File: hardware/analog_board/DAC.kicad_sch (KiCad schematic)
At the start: 20 parts, among them U3 AD9747BCPZ

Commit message: feat: 滤波器&差分转单端电路原理图
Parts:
- added C100, C103, C104, C107, C108, C96: 10uF, Capacitor_SMD:C_0603_1608Metric, symbol Device:C
- added C101, C102, C105, C106, C91, C92, C93, C94, C98, C99: 100nF, Capacitor_SMD:C_0603_1608Metric, symbol Device:C
- added C61, C65, C75, C76: 56pF, Capacitor_SMD:C_0603_1608Metric, symbol Device:C
- added C62, C63, C66, C67, C79, C80, C83, C84: 100pF, Capacitor_SMD:C_0603_1608Metric, symbol Device:C
- added C64, C68, C87, C88: 62pF, Capacitor_SMD:C_0603_1608Metric, symbol Device:C
- added C69, C72, C77, C78: 6.8p, Capacitor_SMD:C_0603_1608Metric, symbol Device:C
- added C70, C73, C81, C82, C90, C95: 9.1p, Capacitor_SMD:C_0603_1608Metric, symbol Device:C
- added C71, C74, C85, C86: 2.0p, Capacitor_SMD:C_0603_1608Metric, symbol Device:C
- added FB10, FB5, FB6, FB7, FB8, FB9: 600R@100MHz, Inductor_SMD:L_0603_1608Metric, symbol Device:FerriteBead_Small
- added L1, L4, L7, L8: 160n, Inductor_SMD:L_0805_2012Metric, symbol Device:L
- added L10, L11, L12, L2, L3, L5, L6, L9: 180n, Inductor_SMD:L_0805_2012Metric, symbol Device:L
- added Q1, Q2: MMBT3906, Package_TO_SOT_SMD:SOT-23, symbol Transistor_BJT:MMBT3906
- added R29, R41: 53.6R, Resistor_SMD:R_0603_1608Metric, symbol Device:R
- added R30, R42: 226R, Resistor_SMD:R_0603_1608Metric, symbol Device:R
- added R31, R32, R43, R44: 73.2R, Resistor_SMD:R_0603_1608Metric, symbol Device:R
- added R33, R34, R45, R46: 442R, Resistor_SMD:R_0603_1608Metric, symbol Device:R
- added R35, R38: 0R, Resistor_SMD:R_0603_1608Metric, symbol Device:R
- added R36, R37, R39, R40: 10kR, Resistor_SMD:R_0603_1608Metric, symbol Device:R
- added R49, R51: 68R, Resistor_SMD:R_0603_1608Metric, symbol Device:R
- added R50, R52: 100R, Resistor_SMD:R_0603_1608Metric, symbol Device:R
- added U4, U5: OPA695ID, Package_SO:SOIC-8_3.9x4.9mm_P1.27mm, symbol ArbWave30_lib:OPA695ID
- added U6, U7: NE5532, symbol Amplifier_Operational:NE5532
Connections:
- net GND: now also C100.1, C101.1, C102.1, C103.1, C104.1, C105.1, C106.1, C107.1, C108.1, C61.1, C64.1, C65.2, C68.2, C75.1, C76.2, C87.1, C88.2, C91.1, C92.1, C93.1, C94.1, C96.1, C98.1, C99.1, R29.2, R30.1, R33.2, R35.1, R38.1, R41.2, R42.1, R45.2, U6.5 (+), U7.5 (+); no longer R22.1, R23.2, R26.1, R27.2
- net at U3.59 (IOUT2P): now also R27.1, C76.1, C78.2, L8.1; no longer R26.2
- net at U3.60 (IOUT2N): now also R26.2, C75.2, C77.2, L7.1; no longer R27.1
- net at R23.1, U3.68 (IOUT1N): now also C65.1, C72.2, L4.1
- net at R22.2, U3.69 (IOUT1P): now also C61.2, C69.2, L1.1
- net CLKN renamed CLK-
- net CLK-: no longer C58.2, R15.1
- net CLKP renamed CLK+
- net CLK+: no longer C57.2, R15.2
- new net: R22.1, R23.2, R35.2, R49.1
- new net: C105.2, C107.2, FB9.2, U6.8 (V+)
- new net: C63.1, C67.2
- new net: C63.2, C70.1, C71.2, L2.2, L3.1
- new net: C100.2, C99.2, FB6.2, U4.4 (V-)
- new net: C85.1, C87.2, L11.2, R39.2, R41.1, R43.1
- new net: R43.2, R45.1, U5.3 (+)
- new net: R44.2, R46.1, U5.2 (-)
- new net: C95.2, R52.1, U7.7
- new net: Q2.1 (B), R52.2
- new net: C101.2, C103.2, FB7.2, U5.7 (V+)
- new net: C81.1, C83.2, C85.2, L11.1, L9.2
- new net: C77.1, C79.2, C81.2, L7.2, L9.1
- new net: C86.1, C88.1, L12.2, R40.1, R42.2, R44.1
- new net: C95.1, R39.1, R40.2, U7.6 (-)
- new net: C91.2, C92.2, Q1.2 (E), R49.2
- new net: C96.2, C98.2, FB5.2, U4.7 (V+)
- new net: C62.2, C69.1, C70.2, L1.2, L2.1
- new net: C78.1, C80.1, C82.2, L10.1, L8.2
- new net: C79.1, C80.2
- new net: C90.2, R50.1, U6.7
- new net: Q1.1 (B), R50.2
- new net: R32.2, R34.1, U4.2 (-)
- new net: R31.2, R33.1, U4.3 (+)
- new net: R26.1, R27.2, R38.2, R51.1
- new net: C64.2, C71.1, L3.2, R29.1, R31.1, R36.2
- new net: C82.1, C84.1, C86.2, L10.2, L12.1
- new net: C83.1, C84.2
- new net: C106.2, C108.2, FB10.2, U6.4 (V-)
- new net: C67.1, C73.1, C74.2, L5.2, L6.1
- new net: C90.1, R36.1, R37.2, U6.6 (-)
- new net: C93.2, C94.2, Q2.2 (E), R51.2
- new net: C62.1, C66.2
- new net: C66.1, C72.1, C73.2, L4.2, L5.1
- new net: C102.2, C104.2, FB8.2, U5.4 (V-)
- new net: C68.1, C74.1, L6.2, R30.2, R32.1, R37.1
- new net +5VA: FB5.1, FB7.1, FB9.1
- new net -5VA: FB10.1, FB6.1, FB8.1, Q1.3 (C), Q2.3 (C)
- new net DAC_CKL_-: C58.2, R15.1
- new net DAC_CLK+: C57.2, R15.2
- new net OUT: R34.2, R46.2, U4.6, U5.6
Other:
- moved on the sheet: C56, C57, C58, C59, C60, R14, R15, R16, R17, R18, R19, R22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

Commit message: feat：时钟电路原理图
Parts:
- C90, C95: value 9.1p -> 100n
- R28: value 0R -> 4.7k
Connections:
- net +1.8VA: no longer U3.1 (CVDD18), U3.6 (CVDD18)
- net +1.8VD renamed +1.8VD_DAC
- net +3.3V renamed +3.3VD_DAC
- net +3.3VA renamed +3.3VA_DAC
- net DAC_CKL_- renamed DAC_CKL-
- net OUT renamed OUT1
- net OUT1: no longer R46.2, U5.6
- new net +1.8VA_DAC: U3.1 (CVDD18), U3.6 (CVDD18)
- new net OUT2: R46.2, U5.6
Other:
- moved on the sheet: C100, C101, C102, C103, C104, C96, C98, C99, FB5, FB6, FB7, FB8

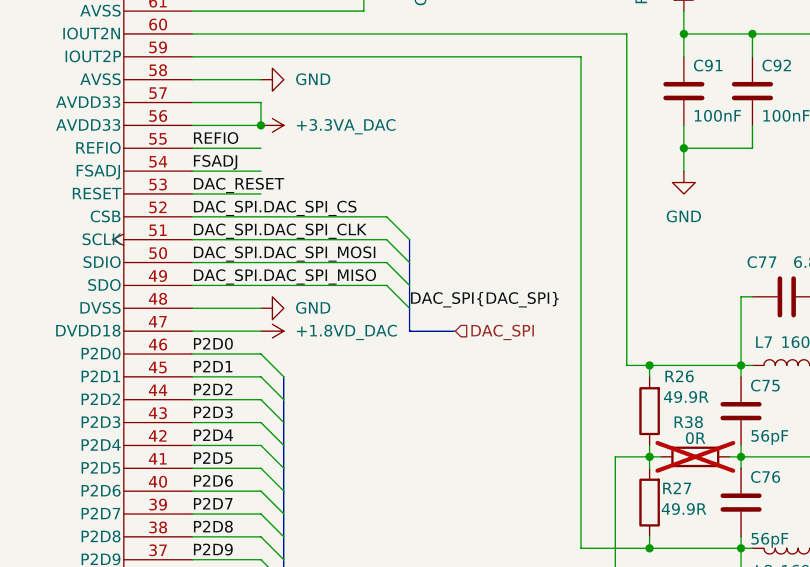
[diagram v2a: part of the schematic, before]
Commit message: feat：完成模拟板板间接口设计
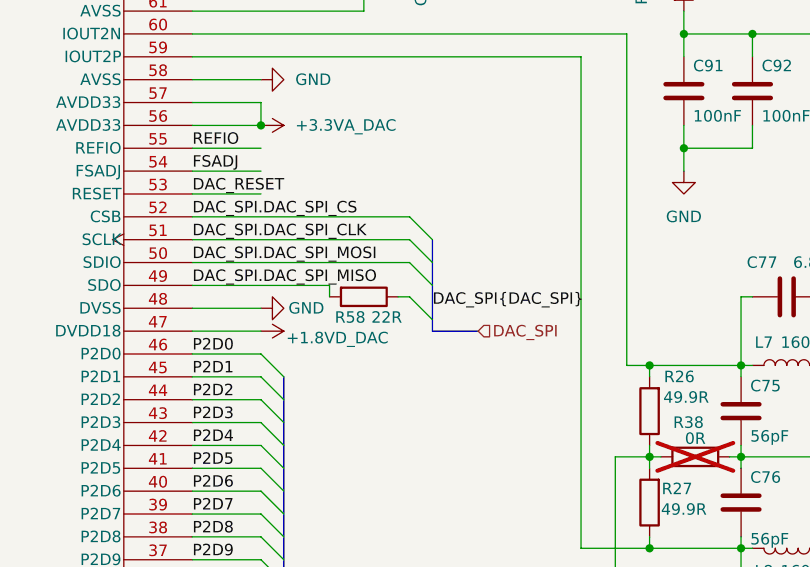
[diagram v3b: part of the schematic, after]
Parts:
- added R58: 22R, Resistor_SMD:R_0402_1005Metric, symbol Device:R
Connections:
- net DAC_SPI.DAC_SPI_MISO: now also R58.2
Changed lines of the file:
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@@
 	)
 	(bus_entry
-		(at 132.08 95.25)
+		(at 134.62 95.25)
 		(size -2.54 -2.54)
 		(stroke
@@
 	)
 	(bus_entry
-		(at 132.08 100.33)
+		(at 134.62 100.33)
 		(size -2.54 -2.54)
 		(stroke
@@
 	)
 	(bus_entry
-		(at 132.08 97.79)
+		(at 134.62 97.79)
 		(size -2.54 -2.54)
 		(stroke
@@
 	)
 	(bus_entry
-		(at 132.08 102.87)
+		(at 134.62 104.14)
 		(size -2.54 -2.54)
 		(stroke
@@
 	(wire
 		(pts
+			(xy 107.95 95.25) (xy 132.08 95.25)
+		)
+		(stroke
+			(width 0)
+			(type default)
+		)
+	)
+	(wire
+		(pts
 			(xy 107.95 67.31) (xy 116.84 67.31)
 		)
@@
 	(wire
 		(pts
-			(xy 107.95 95.25) (xy 129.54 95.25)
-		)
-		(stroke
-			(width 0)
-			(type default)
-		)
-	)
-	(wire
-		(pts
 			(xy 57.15 115.57) (xy 50.8 115.57)
 		)
@@
 	(wire
 		(pts
-			(xy 107.95 100.33) (xy 129.54 100.33)
-		)
-		(stroke
-			(width 0)
-			(type default)
-		)
-	)
-	(wire
-		(pts
 			(xy 210.82 118.11) (xy 210.82 119.38)
 		)
@@
 	(wire
 		(pts
-			(xy 107.95 92.71) (xy 129.54 92.71)
-		)
-		(stroke
-			(width 0)
-			(type default)
-		)
-	)
-	(wire
-		(pts
 			(xy 49.53 39.37) (xy 57.15 39.37)
 		)
@@
 	(wire
 		(pts
+			(xy 130.81 101.6) (xy 132.08 101.6)
+		)
+		(stroke
+			(width 0)
+			(type default)
+		)
+	)
+	(wire
+		(pts
 			(xy 39.37 69.85) (xy 57.15 69.85)
 		)
@@
 	(wire
 		(pts
+			(xy 123.19 101.6) (xy 123.19 100.33)
+		)
+		(stroke
+			(width 0)
+			(type default)
+		)
+	)
+	(wire
+		(pts
 			(xy 210.82 109.22) (xy 219.71 109.22)
 		)
@@
 		)
 	)
-	(bus
-		(pts
-			(xy 132.08 95.25) (xy 132.08 102.87)
-		)
-		(stroke
-			(width 0)
-			(type default)
-		)
-	)
 	(wire
 		(pts
@@
 	(wire
 		(pts
+			(xy 123.19 100.33) (xy 107.95 100.33)
+		)
+		(stroke
+			(width 0)
+			(type default)
+		)
+	)
+	(wire
+		(pts
 			(xy 107.95 90.17) (xy 115.57 90.17)
 		)
@@
 	(wire
 		(pts
-			(xy 57.15 128.27) (xy 50.8 128.27)
+			(xy 107.95 92.71) (xy 132.08 92.71)
 		)
 		(stroke
@@
 	(wire
 		(pts
-			(xy 107.95 97.79) (xy 129.54 97.79)
+			(xy 57.15 128.27) (xy 50.8 128.27)
 		)
 		(stroke
@@
 	(bus
 		(pts
-			(xy 132.08 105.41) (xy 137.16 105.41)
+			(xy 134.62 105.41) (xy 139.7 105.41)
 		)
 		(stroke
@@
 	(bus
 		(pts
-			(xy 132.08 102.87) (xy 132.08 105.41)
+			(xy 134.62 95.25) (xy 134.62 105.41)
 		)
 		(stroke
@@
 	(wire
 		(pts
+			(xy 107.95 97.79) (xy 132.08 97.79)
+		)
+		(stroke
+			(width 0)
+			(type default)
+		)
+	)
+	(wire
+		(pts
 			(xy 186.69 40.64) (xy 186.69 43.18)
 		)
@@
 	)
 	(label "DAC_SPI{DAC_SPI}"
-		(at 132.08 102.87 0)
+		(at 134.62 102.87 0)
 		(effects
 			(font
@@
 	(hierarchical_label "DAC_SPI"
 		(shape input)
-		(at 137.16 105.41 0)
+		(at 139.7 105.41 0)
 		(effects
 			(font
@@
 		(polyline
 			(pts
-				(xy 151.13 99.06) (xy 264.16 99.06) (xy 264.16 143.51) (xy 151.13 143.51)
+				(xy 152.4 99.695) (xy 264.16 99.06) (xy 264.16 143.51) (xy 152.4 144.145)
 			)
 			(stroke
@@
 		(in_pos_files yes)
 		(dnp no)
-		(fields_autoplaced yes)
 		(property "Reference" "#PWR065"
 			(at 111.76 105.41 0)
@@
 		)
 		(property "Value" "+1.8VD_DAC"
-			(at 119.38 105.4099 90)
+			(at 118.364 106.172 90)
 			(show_name no)
 			(do_not_autoplace no)
@@
 		(in_pos_files yes)
 		(dnp no)
-		(fields_autoplaced yes)
 		(property "Reference" "#PWR073"
 			(at 121.92 102.87 0)
@@
 		)
 		(property "Value" "GND"
-			(at 119.38 102.8699 90)
+			(at 118.618 102.87 90)
 			(show_name no)
 			(do_not_autoplace no)
@@
 					(unit 1)
 				)
+			)
+		)
+	)
+	(symbol
+		(lib_id "Device:R")
+		(at 127 101.6 270)
+		(unit 1)
+		(body_style 1)
+		(exclude_from_sim no)
+		(in_bom yes)
+		(on_board yes)
+		(in_pos_files yes)
+		(dnp no)
+		(property "Reference" "R58"
+			(at 125.476 103.886 90)
+			(show_name no)
+			(do_not_autoplace no)
+			(effects
+				(font
+					(size 1.27 1.27)
+				)
+			)
+		)
+		(property "Value" "22R"
+			(at 129.54 103.886 90)
+			(show_name no)
+			(do_not_autoplace no)
+			(effects
+				(font
+					(size 1.27 1.27)
+				)
+			)
+		)
+		(property "Footprint" "Resistor_SMD:R_0402_1005Metric"
+			(at 127 99.822 90)
+			(hide yes)
+			(show_name no)
+			(do_not_autoplace no)
+			(effects
+				(font
+					(size 1.27 1.27)
+				)
+			)
+		)
+		(property "Datasheet" ""
+			(at 127 101.6 0)
+			(hide yes)
+			(show_name no)
+			(do_not_autoplace no)
+			(effects
+				(font
+					(size 1.27 1.27)
+				)
+			)
+		)
+		(property "Description" "Resistor"
+			(at 127 101.6 0)
+			(hide yes)
+			(show_name no)
+			(do_not_autoplace no)
+			(effects
+				(font
+					(size 1.27 1.27)
+				)
+			)
+		)
+		(pin "1"
+		)
+		(pin "2"
+		)
+		(instances
+			(project "analog_board"
+				(path "/ca4be128-f2cd-4bef-b262-ed123f9c630d/0038aa63-4831-4c1d-98ec-8ad35a3c76ff"
+					(reference "R58")
+					(unit 1)
+				)

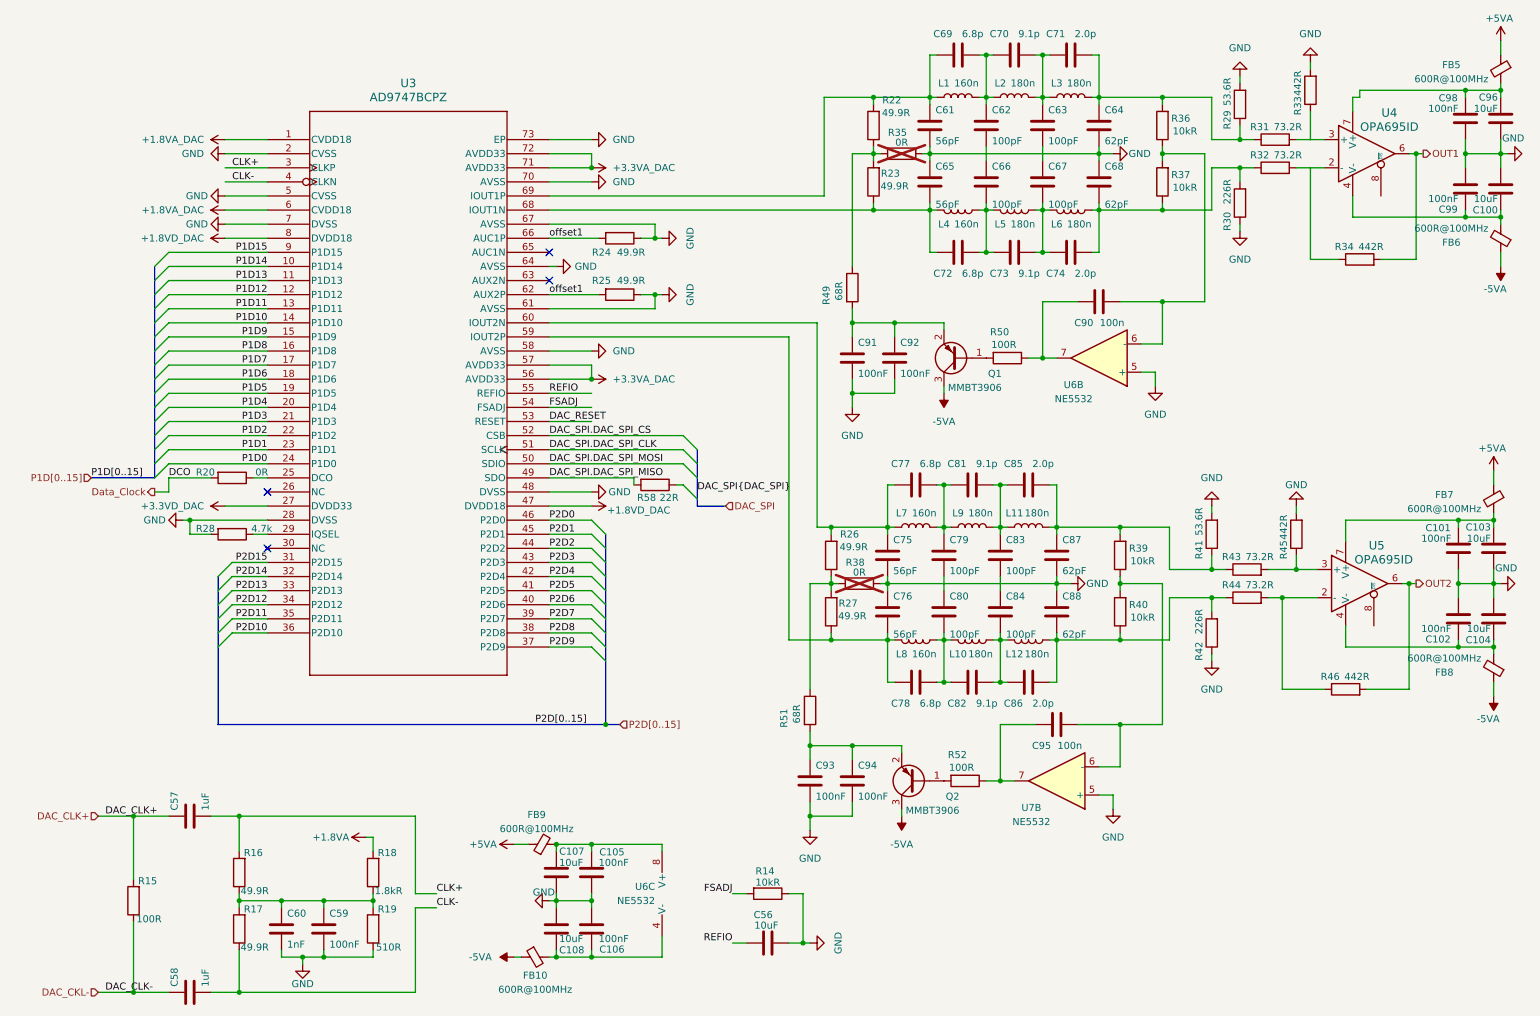
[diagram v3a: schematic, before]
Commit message: feat：模拟板电源 原理图设计
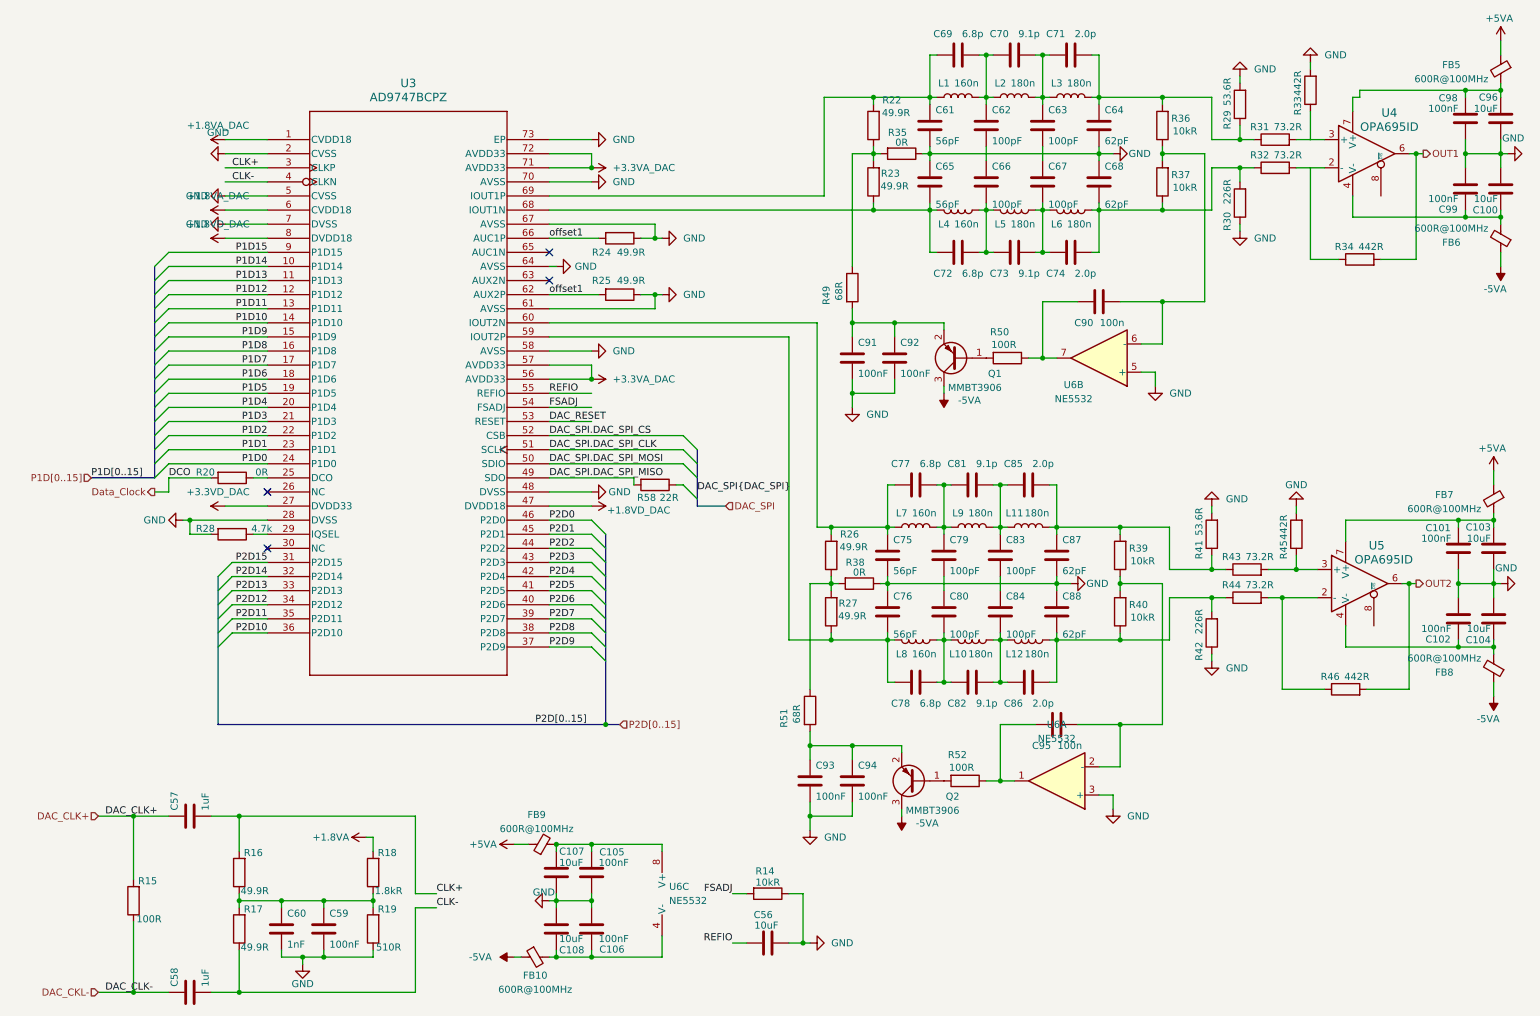
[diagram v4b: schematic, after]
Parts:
- removed U7: NE5532, symbol Amplifier_Operational:NE5532
- added unit 1 of U6
- R35, R38: now fitted
- U6: footprint (none) -> Package_SO:SOIC-8_3.9x4.9mm_P1.27mm
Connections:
- net GND: now also U6.3 (+)
- net at C95.2, R52.1: now also U6.1
- net at C95.1, R39.1, R40.2: now also U6.2 (-)

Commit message: feat：重构滤波器预布局
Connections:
- net GND: now also C62.1, C63.1, C66.2, C67.2, C79.1, C80.2, C83.1, C84.2
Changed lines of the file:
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@@
 	)
 	(junction
-		(at 273.05 30.48)
-		(diameter 0)
-		(color 0 0 0 0)
-	)
-	(junction
 		(at 67.31 176.53)
 		(diameter 0)
@@
 	)
 	(junction
+		(at 179.07 119.38)
+		(diameter 0)
+		(color 0 0 0 0)
+	)
+	(junction
 		(at 218.44 52.07)
 		(diameter 0)
@@
 	)
 	(junction
+		(at 273.05 30.48)
+		(diameter 0)
+		(color 0 0 0 0)
+	)
+	(junction
 		(at 196.85 31.75)
 		(diameter 0)
@@
 	)
 	(junction
+		(at 186.69 41.91)
+		(diameter 0)
+		(color 0 0 0 0)
+	)
+	(junction
 		(at 168.91 129.54)
 		(diameter 0)
@@
 	)
 	(junction
+		(at 189.23 119.38)
+		(diameter 0)
+		(color 0 0 0 0)
+	)
+	(junction
 		(at 279.4 41.91)
 		(diameter 0)
@@
 	)
 	(junction
+		(at 196.85 41.91)
+		(diameter 0)
+		(color 0 0 0 0)
+	)
+	(junction
 		(at 162.56 148.59)
 		(diameter 0)
@@
 	(wire
 		(pts
+			(xy 186.69 41.91) (xy 196.85 41.91)
+		)
+		(stroke
+			(width 0)
+			(type default)
+		)
+	)
+	(wire
+		(pts
 			(xy 262.89 41.91) (xy 264.16 41.91)
 		)
@@
 	(wire
 		(pts
+			(xy 179.07 119.38) (xy 189.23 119.38)
+		)
+		(stroke
+			(width 0)
+			(type default)
+		)
+	)
+	(wire
+		(pts
 			(xy 158.75 119.38) (xy 154.94 119.38)
 		)
@@
 	(wire
 		(pts
-			(xy 254 31.75) (xy 252.73 31.75)
+			(xy 189.23 119.38) (xy 189.23 120.65)
 		)
 		(stroke
@@
 	(wire
 		(pts
-			(xy 189.23 118.11) (xy 189.23 120.65)
+			(xy 189.23 118.11) (xy 189.23 119.38)
 		)
 		(stroke
@@
 	(wire
 		(pts
-			(xy 196.85 40.64) (xy 196.85 43.18)
+			(xy 196.85 40.64) (xy 196.85 41.91)
 		)
 		(stroke
@@
 	(wire
 		(pts
-			(xy 179.07 118.11) (xy 179.07 120.65)
+			(xy 179.07 118.11) (xy 179.07 119.38)
 		)
 		(stroke
@@
 	(wire
 		(pts
-			(xy 176.53 41.91) (xy 207.01 41.91)
+			(xy 176.53 41.91) (xy 186.69 41.91)
 		)
 		(stroke
@@
 	(wire
 		(pts
+			(xy 189.23 119.38) (xy 199.39 119.38)
+		)
+		(stroke
+			(width 0)
+			(type default)
+		)
+	)
+	(wire
+		(pts
 			(xy 107.95 130.81) (xy 115.57 130.81)
 		)
@@
 	(wire
 		(pts
-			(xy 107.95 186.69) (xy 109.22 186.69)
+			(xy 186.69 41.91) (xy 186.69 43.18)
 		)
 		(stroke
@@
 	(wire
 		(pts
-			(xy 189.23 109.22) (xy 189.23 110.49)
+			(xy 107.95 186.69) (xy 109.22 186.69)
 		)
 		(stroke
@@
 	(wire
 		(pts
-			(xy 109.22 175.26) (xy 109.22 176.53)
+			(xy 189.23 109.22) (xy 189.23 110.49)
 		)
 		(stroke
@@
 	(wire
 		(pts
-			(xy 179.07 129.54) (xy 180.34 129.54)
+			(xy 109.22 175.26) (xy 109.22 176.53)
 		)
 		(stroke
@@
 	(wire
 		(pts
-			(xy 207.01 50.8) (xy 207.01 52.07)
+			(xy 179.07 129.54) (xy 180.34 129.54)
 		)
 		(stroke
@@
 	(wire
 		(pts
-			(xy 252.73 31.75) (xy 252.73 34.29)
+			(xy 207.01 50.8) (xy 207.01 52.07)
 		)
 		(stroke
@@
 	(wire
 		(pts
-			(xy 254 30.48) (xy 273.05 30.48)
+			(xy 252.73 30.48) (xy 273.05 30.48)
 		)
 		(stroke
@@
 	(wire
 		(pts
-			(xy 254 30.48) (xy 254 31.75)
+			(xy 252.73 30.48) (xy 252.73 34.29)
 		)
 		(stroke
@@
 	(wire
 		(pts
+			(xy 196.85 41.91) (xy 196.85 43.18)
+		)
+		(stroke
+			(width 0)
+			(type default)
+		)
+	)
+	(wire
+		(pts
 			(xy 210.82 119.38) (xy 210.82 120.65)
 		)
@@
 	(wire
 		(pts
+			(xy 179.07 119.38) (xy 179.07 120.65)
+		)
+		(stroke
+			(width 0)
+			(type default)
+		)
+	)
+	(wire
+		(pts
 			(xy 115.57 177.8) (xy 115.57 176.53)
 		)
@@
 	(wire
 		(pts
+			(xy 196.85 41.91) (xy 207.01 41.91)
+		)
+		(stroke
+			(width 0)
+			(type default)
+		)
+	)
+	(wire
+		(pts
 			(xy 226.06 41.91) (xy 226.06 68.58)
 		)
@@
 	(wire
 		(pts
-			(xy 168.91 119.38) (xy 199.39 119.38)
+			(xy 168.91 119.38) (xy 179.07 119.38)
 		)
 		(stroke
@@
 	(wire
 		(pts
-			(xy 186.69 40.64) (xy 186.69 43.18)
+			(xy 186.69 40.64) (xy 186.69 41.91)
 		)
 		(stroke
@@
 		(polyline
 			(pts
-				(xy 151.765 19.05) (xy 264.795 19.05) (xy 265.43 63.5) (xy 152.4 63.5)
+				(xy 152.4 19.05) (xy 265.43 19.05) (xy 265.43 63.5) (xy 152.4 63.5)
 			)
 			(stroke
@@
 		(in_pos_files yes)
 		(dnp no)
-		(fields_autoplaced yes)
 		(property "Reference" "#PWR060"
 			(at 53.34 57.15 0)
@@
 		)
 		(property "Value" "+1.8VD_DAC"
-			(at 48.26 54.61 90)
+			(at 41.148 57.15 90)
 			(show_name no)
 			(do_not_autoplace no)
@@
 		(in_pos_files yes)
 		(dnp no)
-		(fields_autoplaced yes)
 		(property "Reference" "U6"
-			(at 199.39 144.78 0)
+			(at 193.294 158.242 0)
 			(show_name no)
 			(do_not_autoplace no)
@@
 		)
 		(property "Value" "NE5532"
-			(at 199.39 147.32 0)
+			(at 193.294 160.782 0)
 			(show_name no)
 			(do_not_autoplace no)
@@
 		(in_pos_files yes)
 		(dnp no)
-		(fields_autoplaced yes)
 		(property "Reference" "#PWR042"
 			(at 53.34 52.07 0)
@@
 		)
 		(property "Value" "+1.8VA_DAC"
-			(at 48.26 49.53 90)
+			(at 41.148 52.07 90)
 			(show_name no)
 			(do_not_autoplace no)
